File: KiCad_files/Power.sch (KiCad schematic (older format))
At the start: 101 parts, among them J2 PCIe_6_Pin_Power, Q1 Q_NMOS_DGS, Q2 Q_PMOS_DGS, U1 XC7A35T_CSG325, U13 LM2676, U2 MAX15027, U3 PI3420, U4 PI3421, U5 PI3420

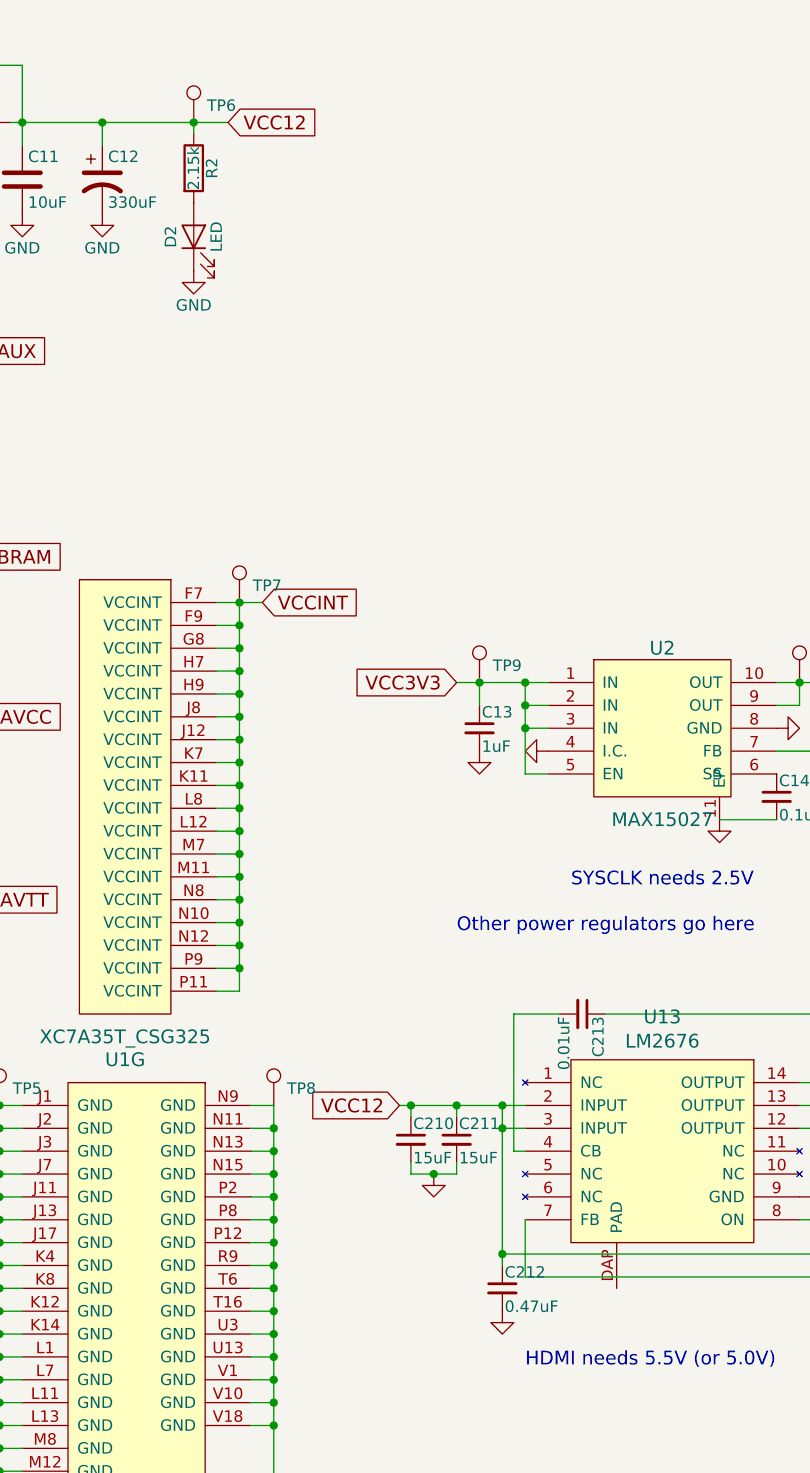
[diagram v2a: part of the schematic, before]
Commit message: Almost done with footprints. See issues below
Inductors left to do.
Others without footprints need custom.
PI3420 is out of stock...
LM2676 symbol should be re-drawn for TO-263-7
Total cost: ~$214
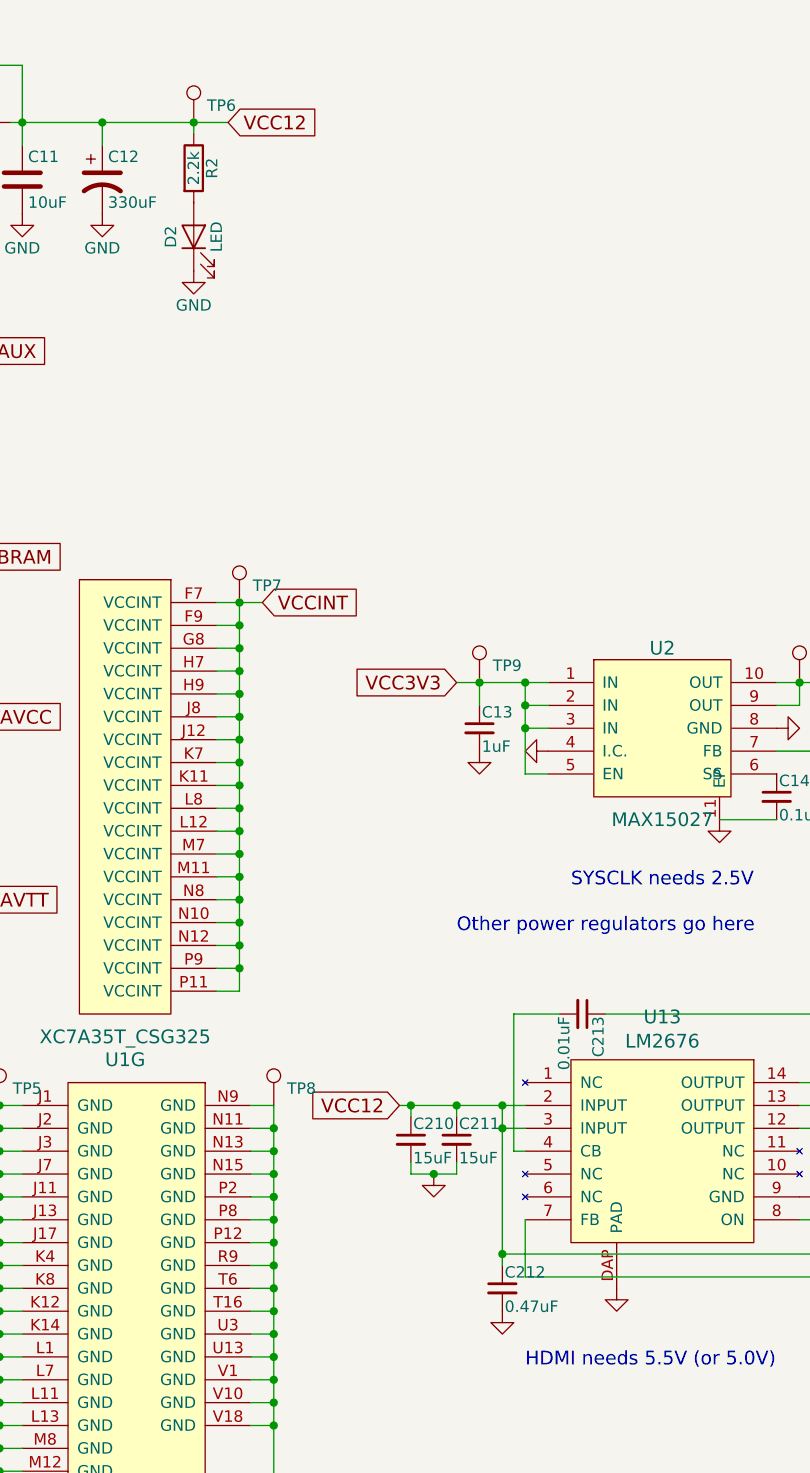
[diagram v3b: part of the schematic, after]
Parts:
- D1, D8: footprint (none) -> Diodes_SMD:D_SOD-123
- D2: footprint (none) -> LEDs:LED_0603
- J2: footprint (none) -> Connectors_Molex:Molex_MiniFit-JR-5569-06A2_2x03x4.20mm_Angled
- R2: value 2.15k -> 2.2k; footprint (none) -> Resistors_SMD:R_0402
- R3, R4, R6: footprint (none) -> Resistors_SMD:R_0402
- R5: footprint (none) -> Resistors_SMD:R_0603
- TP1, TP10, TP11, TP12, TP13, TP14, TP15, TP16, TP17, TP2, TP3, TP4, TP5, TP6, TP7, TP8, TP9: footprint (none) -> Measurement_Points:Measurement_Point_Round-SMD-Pad_Small
- U13: footprint (none) -> TO_SOT_Packages_SMD:TO-263-7_TabPin8
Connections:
- net GND: now also U13.DAP (PAD)
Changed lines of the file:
@@
 F 0 "D1" H 1900 1100 50  0000 C CNN
 F 1 "D_Zener" H 1900 900 50  0001 C CNN
-F 2 "" H 1900 1000 50  0001 C CNN
+F 2 "Diodes_SMD:D_SOD-123" H 1900 1000 50  0001 C CNN
 F 3 "" H 1900 1000 50  0001 C CNN
 	1    1900 1000
@@
 F 0 "D2" H 2850 1600 50  0000 C CNN
 F 1 "LED" H 2850 1400 50  0000 C CNN
-F 2 "" H 2850 1500 50  0001 C CNN
+F 2 "LEDs:LED_0603" H 2850 1500 50  0001 C CNN
 F 3 "" H 2850 1500 50  0001 C CNN
 	1    2850 1500
@@
 P 2850 1200
 F 0 "R2" V 2930 1200 50  0000 C CNN
-F 1 "2.15k" V 2850 1200 50  0000 C CNN
-F 2 "" V 2780 1200 50  0001 C CNN
+F 1 "2.2k" V 2850 1200 50  0000 C CNN
+F 2 "Resistors_SMD:R_0402" V 2780 1200 50  0001 C CNN
 F 3 "" H 2850 1200 50  0001 C CNN
 	1    2850 1200
@@
 F 0 "J2" H 1100 1650 60  0000 C CNN
 F 1 "PCIe_6_Pin_Power" H 1100 850 60  0000 C CNN
-F 2 "" H 1100 1250 60  0001 C CNN
+F 2 "Connectors_Molex:Molex_MiniFit-JR-5569-06A2_2x03x4.20mm_Angled" H 1100 1250 60  0001 C CNN
 F 3 "" H 1100 1250 60  0001 C CNN
 	1    1100 1250
@@
 Text GLabel 8800 850  0    60   Input ~ 0
 SGND_PI3420_1
-NoConn ~ 9900 1200
 NoConn ~ 9900 1300
 NoConn ~ 9900 1400
@@
 F 0 "R6" V 10330 4500 50  0000 C CNN
 F 1 "5k" V 10250 4500 50  0000 C CNN
-F 2 "" V 10180 4500 50  0001 C CNN
+F 2 "Resistors_SMD:R_0402" V 10180 4500 50  0001 C CNN
 F 3 "" H 10250 4500 50  0001 C CNN
 	1    10250 4500
@@
 F 0 "R5" V 9380 5500 50  0000 C CNN
 F 1 "1M" V 9300 5500 50  0000 C CNN
-F 2 "" V 9230 5500 50  0001 C CNN
+F 2 "Resistors_SMD:R_0603" V 9230 5500 50  0001 C CNN
 F 3 "" H 9300 5500 50  0001 C CNN
 	1    9300 5500
@@
 	9900 1000 10000 1000
 Wire Wire Line
-	10000 1100 9900 1100
-Wire Wire Line
 	10000 1500 9950 1500
 Wire Wire Line
@@
 F 0 "R3" V 5730 3600 50  0000 C CNN
 F 1 "40.2k" V 5650 3600 50  0000 C CNN
-F 2 "" V 5580 3600 50  0001 C CNN
+F 2 "Resistors_SMD:R_0402" V 5580 3600 50  0001 C CNN
 F 3 "" H 5650 3600 50  0001 C CNN
 	1    5650 3600
@@
 F 0 "R4" V 5730 3900 50  0000 C CNN
 F 1 "10k" V 5650 3900 50  0000 C CNN
-F 2 "" V 5580 3900 50  0001 C CNN
+F 2 "Resistors_SMD:R_0402" V 5580 3900 50  0001 C CNN
 F 3 "" H 5650 3900 50  0001 C CNN
 	1    5650 3900
@@
 F 0 "U13" H 4900 6487 60  0000 C CNN
 F 1 "LM2676" H 4900 6381 60  0000 C CNN
-F 2 "" H 4900 5850 60  0001 C CNN
+F 2 "TO_SOT_Packages_SMD:TO-263-7_TabPin8" H 4900 5850 60  0001 C CNN
 F 3 "" H 4900 5850 60  0001 C CNN
 	1    4900 5700
@@
 F 0 "D8" V 5700 5479 50  0000 L CNN
 F 1 "D_Schottky" V 5745 5479 50  0001 L CNN
-F 2 "" H 5700 5400 50  0001 C CNN
+F 2 "Diodes_SMD:D_SOD-123" H 5700 5400 50  0001 C CNN
 F 3 "~" H 5700 5400 50  0001 C CNN
 	1    5700 5400
@@
 F 0 "TP6" H 2908 1074 50  0000 L CNN
 F 1 "TestPoint" H 2908 1029 50  0001 L CNN
-F 2 "" H 3050 1000 50  0001 C CNN
+F 2 "Measurement_Points:Measurement_Point_Round-SMD-Pad_Small" H 3050 1000 50  0001 C CNN
 F 3 "~" H 3050 1000 50  0001 C CNN
 	1    2850 1000
@@
 F 0 "TP1" H 1708 2074 50  0000 L CNN
 F 1 "TestPoint" H 1708 2029 50  0001 L CNN
-F 2 "" H 1850 2000 50  0001 C CNN
+F 2 "Measurement_Points:Measurement_Point_Round-SMD-Pad_Small" H 1850 2000 50  0001 C CNN
 F 3 "~" H 1850 2000 50  0001 C CNN
 	1    1650 2000
@@
 F 0 "TP2" H 1708 2974 50  0000 L CNN
 F 1 "TestPoint" H 1708 2929 50  0001 L CNN
-F 2 "" H 1850 2900 50  0001 C CNN
+F 2 "Measurement_Points:Measurement_Point_Round-SMD-Pad_Small" H 1850 2900 50  0001 C CNN
 F 3 "~" H 1850 2900 50  0001 C CNN
 	1    1650 2900
@@
 F 0 "TP3" H 1708 3674 50  0000 L CNN
 F 1 "TestPoint" H 1708 3629 50  0001 L CNN
-F 2 "" H 1850 3600 50  0001 C CNN
+F 2 "Measurement_Points:Measurement_Point_Round-SMD-Pad_Small" H 1850 3600 50  0001 C CNN
 F 3 "~" H 1850 3600 50  0001 C CNN
 	1    1650 3600
@@
 F 0 "TP4" H 1708 4474 50  0000 L CNN
 F 1 "TestPoint" H 1708 4429 50  0001 L CNN
-F 2 "" H 1850 4400 50  0001 C CNN
+F 2 "Measurement_Points:Measurement_Point_Round-SMD-Pad_Small" H 1850 4400 50  0001 C CNN
 F 3 "~" H 1850 4400 50  0001 C CNN
 	1    1650 4400
@@
 F 0 "TP7" H 3108 3174 50  0000 L CNN
 F 1 "TestPoint" H 3108 3129 50  0001 L CNN
-F 2 "" H 3250 3100 50  0001 C CNN
+F 2 "Measurement_Points:Measurement_Point_Round-SMD-Pad_Small" H 3250 3100 50  0001 C CNN
 F 3 "~" H 3250 3100 50  0001 C CNN
 	1    3050 3100
@@
 F 0 "TP9" H 4158 3524 50  0000 L CNN
 F 1 "TestPoint" H 4158 3479 50  0001 L CNN
-F 2 "" H 4300 3450 50  0001 C CNN
+F 2 "Measurement_Points:Measurement_Point_Round-SMD-Pad_Small" H 4300 3450 50  0001 C CNN
 F 3 "~" H 4300 3450 50  0001 C CNN
 	1    4100 3450
@@
 F 0 "TP10" H 5558 3524 50  0000 L CNN
 F 1 "TestPoint" H 5558 3479 50  0001 L CNN
-F 2 "" H 5700 3450 50  0001 C CNN
+F 2 "Measurement_Points:Measurement_Point_Round-SMD-Pad_Small" H 5700 3450 50  0001 C CNN
 F 3 "~" H 5700 3450 50  0001 C CNN
 	1    5500 3450
@@
 F 0 "TP11" H 6158 5274 50  0000 L CNN
 F 1 "TestPoint" H 6158 5229 50  0001 L CNN
-F 2 "" H 6300 5200 50  0001 C CNN
+F 2 "Measurement_Points:Measurement_Point_Round-SMD-Pad_Small" H 6300 5200 50  0001 C CNN
 F 3 "~" H 6300 5200 50  0001 C CNN
 	1    6100 5200
@@
 F 0 "TP8" H 3258 5374 50  0000 L CNN
 F 1 "TestPoint" H 3258 5329 50  0001 L CNN
-F 2 "" H 3400 5300 50  0001 C CNN
+F 2 "Measurement_Points:Measurement_Point_Round-SMD-Pad_Small" H 3400 5300 50  0001 C CNN
 F 3 "~" H 3400 5300 50  0001 C CNN
 	1    3200 5300
@@
 F 0 "TP5" H 2058 5374 50  0000 L CNN
 F 1 "TestPoint" H 2058 5329 50  0001 L CNN
-F 2 "" H 2200 5300 50  0001 C CNN
+F 2 "Measurement_Points:Measurement_Point_Round-SMD-Pad_Small" H 2200 5300 50  0001 C CNN
 F 3 "~" H 2200 5300 50  0001 C CNN
 	1    2000 5300
@@
 F 0 "TP16" H 9758 5324 50  0000 L CNN
 F 1 "TestPoint" H 9758 5279 50  0001 L CNN
-F 2 "" H 9900 5250 50  0001 C CNN
+F 2 "Measurement_Points:Measurement_Point_Round-SMD-Pad_Small" H 9900 5250 50  0001 C CNN
 F 3 "~" H 9900 5250 50  0001 C CNN
 	1    9700 5250
@@
 F 0 "TP15" V 9403 5774 50  0000 C CNN
 F 1 "TestPoint" H 9358 5729 50  0001 L CNN
-F 2 "" H 9500 5700 50  0001 C CNN
+F 2 "Measurement_Points:Measurement_Point_Round-SMD-Pad_Small" H 9500 5700 50  0001 C CNN
 F 3 "~" H 9500 5700 50  0001 C CNN
 	1    9300 5700
@@
 F 0 "TP17" H 9908 6024 50  0000 L CNN
 F 1 "TestPoint" H 9908 5979 50  0001 L CNN
-F 2 "" H 10050 5950 50  0001 C CNN
+F 2 "Measurement_Points:Measurement_Point_Round-SMD-Pad_Small" H 10050 5950 50  0001 C CNN
 F 3 "~" H 10050 5950 50  0001 C CNN
 	1    9850 5950
@@
 F 0 "TP12" H 6808 1674 50  0000 L CNN
 F 1 "TestPoint" H 6808 1629 50  0001 L CNN
-F 2 "" H 6950 1600 50  0001 C CNN
+F 2 "Measurement_Points:Measurement_Point_Round-SMD-Pad_Small" H 6950 1600 50  0001 C CNN
 F 3 "~" H 6950 1600 50  0001 C CNN
 	1    6750 1600
@@
 F 0 "TP13" H 6808 3274 50  0000 L CNN
 F 1 "TestPoint" H 6808 3229 50  0001 L CNN
-F 2 "" H 6950 3200 50  0001 C CNN
+F 2 "Measurement_Points:Measurement_Point_Round-SMD-Pad_Small" H 6950 3200 50  0001 C CNN
 F 3 "~" H 6950 3200 50  0001 C CNN
 	1    6750 3200
@@
 F 0 "TP14" H 6808 4874 50  0000 L CNN
 F 1 "TestPoint" H 6808 4829 50  0001 L CNN
-F 2 "" H 6950 4800 50  0001 C CNN
+F 2 "Measurement_Points:Measurement_Point_Round-SMD-Pad_Small" H 6950 4800 50  0001 C CNN
 F 3 "~" H 6950 4800 50  0001 C CNN
 	1    6750 4800
@@
 Wire Wire Line
 	9850 5950 9900 5950
+$Comp
+L power:GND #PWR0142
+U 1 1 5C7CA813
+P 4700 6100
+F 0 "#PWR0142" H 4700 5850 50  0001 C CNN
+F 1 "GND" H 4700 5950 50  0001 C CNN
+F 2 "" H 4700 6100 50  0001 C CNN
+F 3 "" H 4700 6100 50  0001 C CNN
+	1    4700 6100
+	1    0    0    -1
+$EndComp
+Wire Wire Line
+	10000 1100 9900 1100
+NoConn ~ 9900 1200
 $EndSCHEMATC
